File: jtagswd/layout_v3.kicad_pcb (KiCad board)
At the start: 2 copper layers, 38.1 x 58.4 mm, 5 parts

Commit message: Minor changes after first combine
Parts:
- DJ1: value Conn_02x05_Odd_Even -> JTAG
- DSW1: value SW_Push -> RESET
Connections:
- DJ1 pad 5: (no net) -> Net-(DJ1-Pad5)
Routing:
- net VDD: track 29.3 -> 37.7 mm
- net ~SRST: track 24.6 -> 28.6 mm, vias 2 -> 1
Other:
- board outline removed
- board text added: "5V"
- board text added: "CLK"
- board text added: "GND"
- board text added: "IO"
- board text added: "VDD"

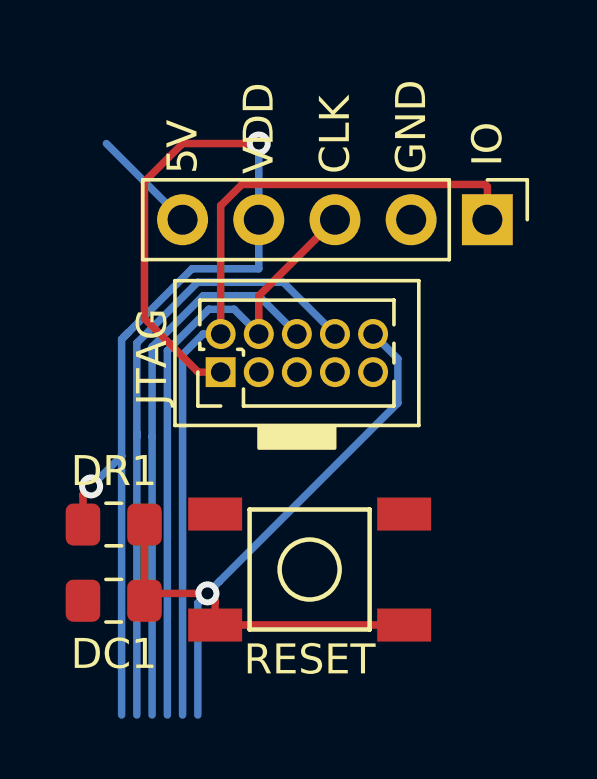
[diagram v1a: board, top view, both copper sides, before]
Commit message: Defining areas and connections per 'module'
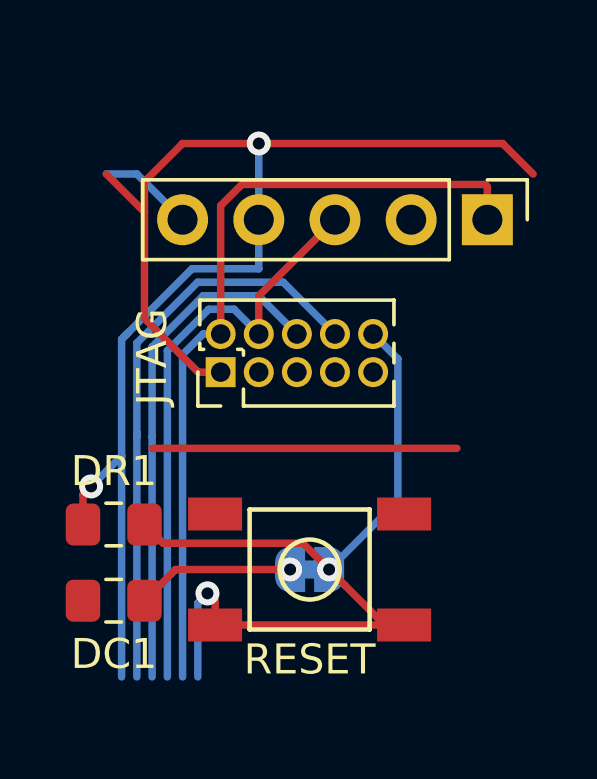
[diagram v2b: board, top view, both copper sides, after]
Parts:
- added DJP1: SolderJumper_2_Bridged, Jumper:SolderJumper-2_P1.3mm_Bridged_RoundedPad1.0x1.5mm, B.Cu at (156.6, 67.5)
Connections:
- DC1 pad 2: ~SRST -> Net-(DC1-Pad2)
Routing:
- net (no net): track 0.00 -> 10.2 mm
- net VDD: track 37.7 -> 47.8 mm
- net Net-(DC1-Pad2): track 0.00 -> 5.29 mm, vias 0 -> 1
- net ~SRST: track 28.6 -> 30.3 mm, vias 1 -> 2
- net TCK: track 21.0 -> 19.7 mm
- net TMS: track 28.2 -> 26.9 mm
- net TDO: track 18.3 -> 17.1 mm
- net TDI: track 20.7 -> 19.4 mm
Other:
- board text removed: "5V"
- board text removed: "CLK"
- board text removed: "GND"
- board text removed: "IO"
- board text removed: "VDD"
